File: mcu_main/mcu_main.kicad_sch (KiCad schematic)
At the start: 23 parts, among them SW1 SW_Push_Dual, SW2 SW_Push_Dual, U1 ESP32-S3-WROOM-1, U3 SGM2212-3.3, U5 SGM2212-2.8

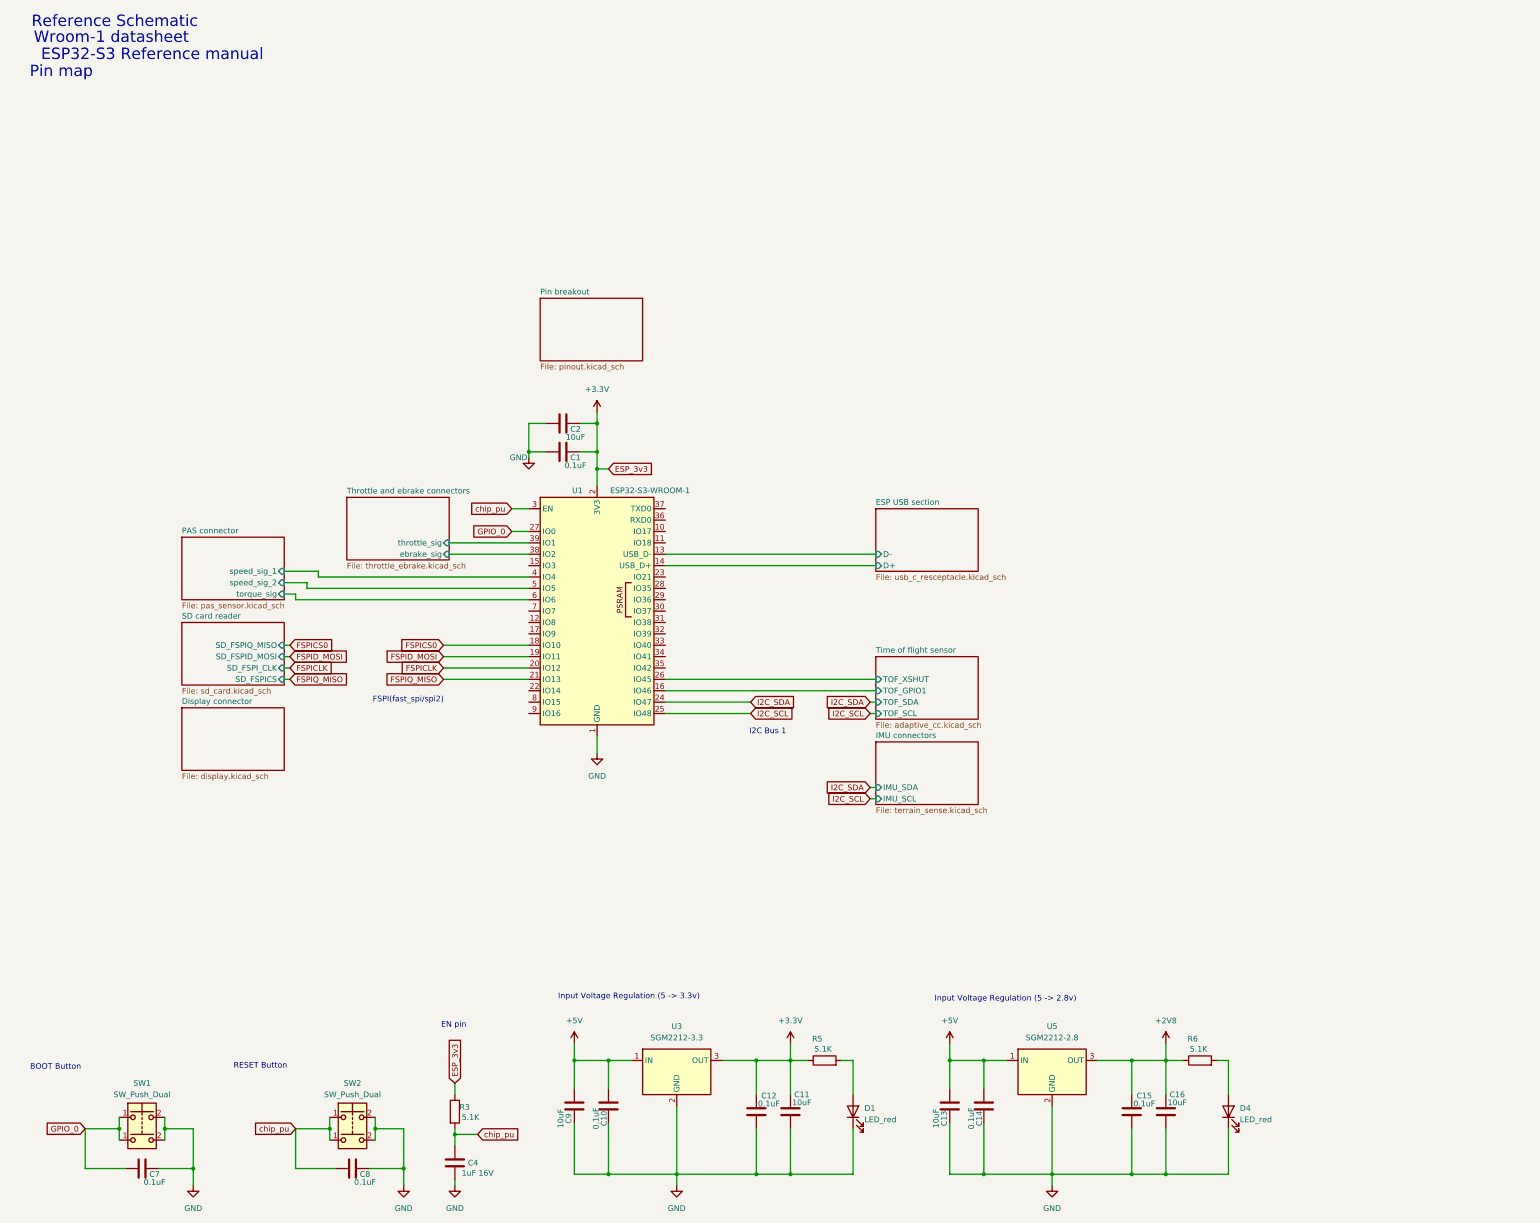
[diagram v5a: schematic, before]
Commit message: Added connections for the display SPI
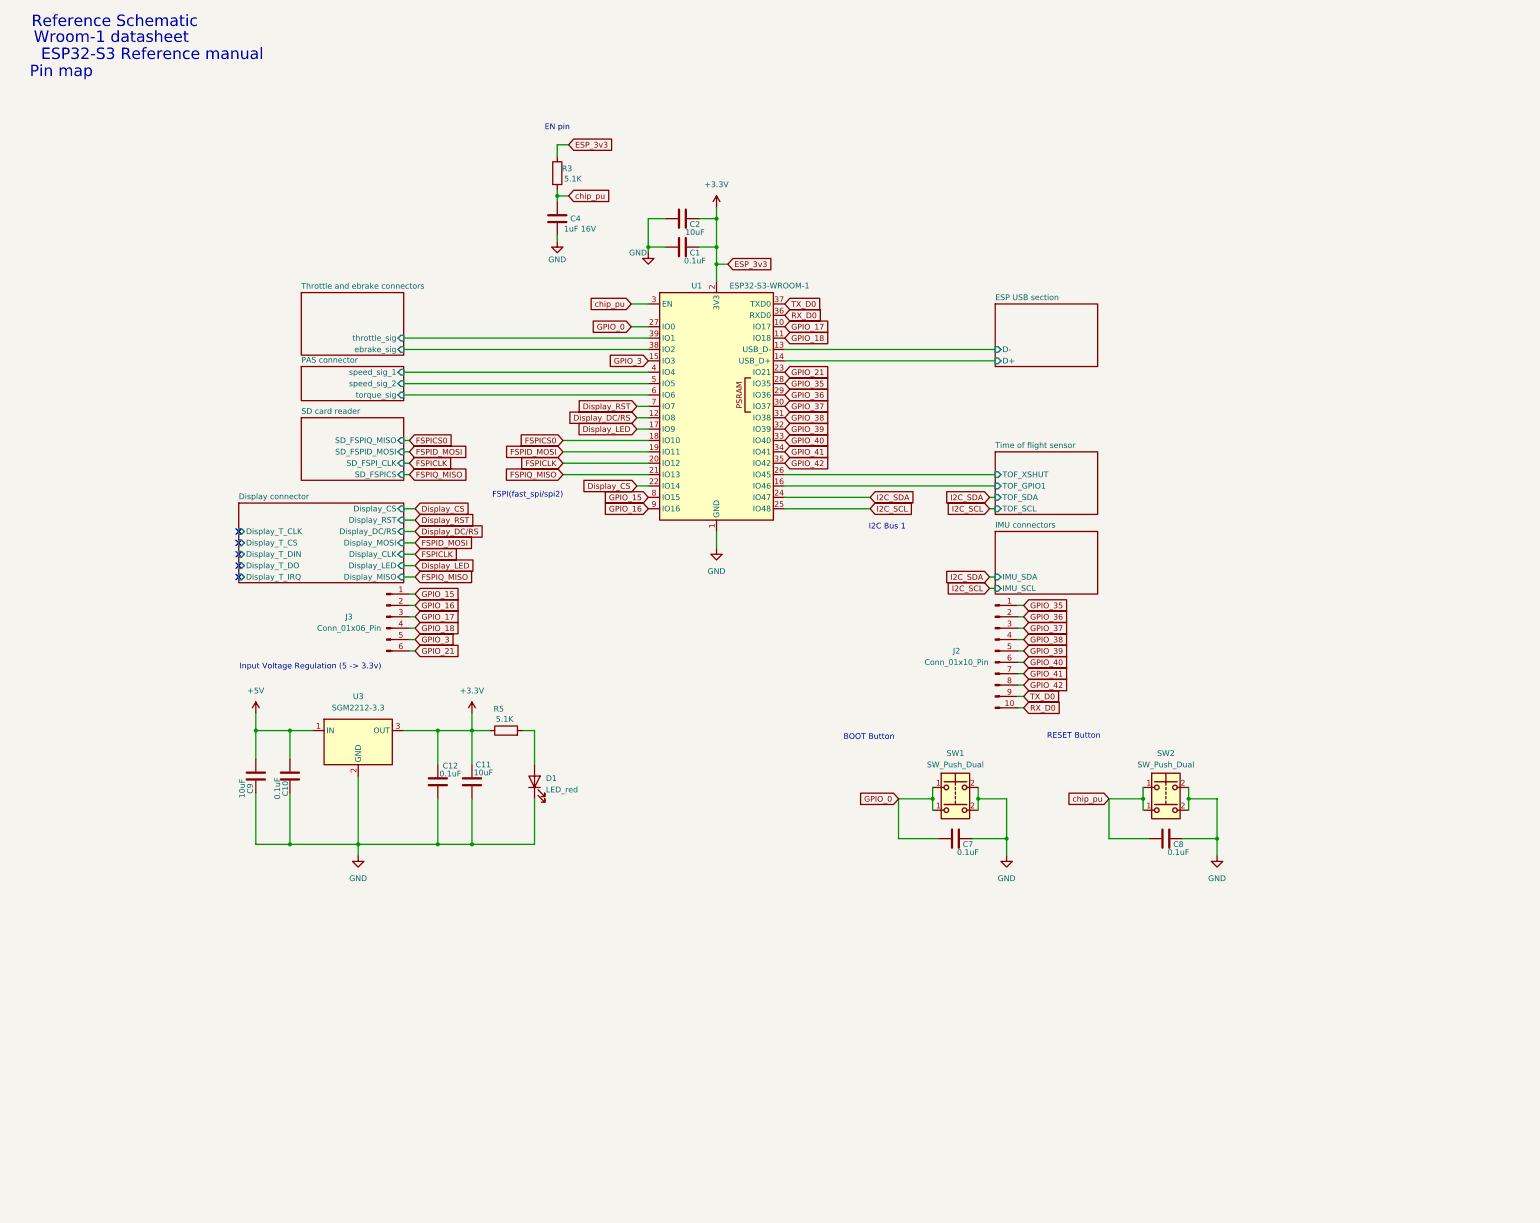
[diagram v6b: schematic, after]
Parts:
- removed C13, C16: 10uF, Capacitor_SMD:C_0603_1608Metric_Pad1.08x0.95mm_HandSolder, symbol Device:C
- removed C14, C15: 0.1uF, Capacitor_SMD:C_0603_1608Metric_Pad1.08x0.95mm_HandSolder, symbol Device:C
- removed D4: LED_red, LED_SMD:LED_0603_1608Metric_Pad1.05x0.95mm_HandSolder, symbol Device:LED
- removed R6: 5.1K, Resistor_SMD:R_0805_2012Metric_Pad1.20x1.40mm_HandSolder, symbol Device:R
- removed U5: SGM2212-2.8, Package_TO_SOT_SMD:SOT-223-3_TabPin2, symbol Regulator_Linear:LT1963AxST-1.5
- added J2: Conn_01x10_Pin, Connector_Molex:Molex_KK-254_AE-6410-10A_1x10_P2.54mm_Vertical, symbol Connector:Conn_01x10_Pin
- added J3: Conn_01x06_Pin, Connector_Molex:Molex_KK-254_AE-6410-06A_1x06_P2.54mm_Vertical, symbol Connector:Conn_01x06_Pin
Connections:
- net GPIO_17: now reaches U1.10 (IO17)
- net GPIO_17: now also J3.3 (Pin_3)
- net GPIO_18: now reaches U1.11 (IO18)
- net GPIO_18: now also J3.4 (Pin_4)
- net Display_DC/RS: now reaches U1.12 (IO8)
- net GPIO_3: now reaches U1.15 (IO3)
- net GPIO_3: now also J3.5 (Pin_5)
- net Display_LED: now reaches U1.17 (IO9)
- net Display_CS: now reaches U1.22 (IO14)
- net GPIO_21: now reaches U1.23 (IO21)
- net GPIO_21: now also J3.6 (Pin_6)
- net GPIO_35: now reaches U1.28 (IO35)
- net GPIO_35: now also J2.1 (Pin_1)
- net GPIO_36: now reaches U1.29 (IO36)
- net GPIO_36: now also J2.2 (Pin_2)
- net GPIO_37: now reaches U1.30 (IO37)
- net GPIO_37: now also J2.3 (Pin_3)
- net GPIO_38: now reaches U1.31 (IO38)
- net GPIO_38: now also J2.4 (Pin_4)
- net GPIO_39: now reaches U1.32 (IO39)
- net GPIO_39: now also J2.5 (Pin_5)
- net GPIO_40: now reaches U1.33 (IO40)
- net GPIO_40: now also J2.6 (Pin_6)
- net GPIO_41: now reaches U1.34 (IO41)
- net GPIO_41: now also J2.7 (Pin_7)
- net GPIO_42: now reaches U1.35 (IO42)
- net GPIO_42: now also J2.8 (Pin_8)
- net RX_D0: now reaches U1.36 (RXD0)
- net RX_D0: now also J2.10 (Pin_10)
- net TX_D0: now reaches U1.37 (TXD0)
- net TX_D0: now also J2.9 (Pin_9)
- net Display_RST: now reaches U1.7 (IO7)
- net GPIO_15: now reaches U1.8 (IO15)
- net GPIO_15: now also J3.1 (Pin_1)
- net GPIO_16: now reaches U1.9 (IO16)
- net GPIO_16: now also J3.2 (Pin_2)
- no-connect marks 0 -> 5
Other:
- removed sheet Pin breakout
- sheet Display connector ports: added Display_CLK, Display_CS, Display_DC/RS, Display_LED, Display_MISO, Display_MOSI, Display_RST, Display_T_CLK, Display_T_CS, Display_T_DIN, Display_T_DO, Display_T_IRQ; removed none
- note removed: "Input Voltage Regulation (5 -> 2.8v)"
- moved on the sheet: C1, C10, C11, C12, C2, C4, C7, C8, C9, D1, R3, R5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

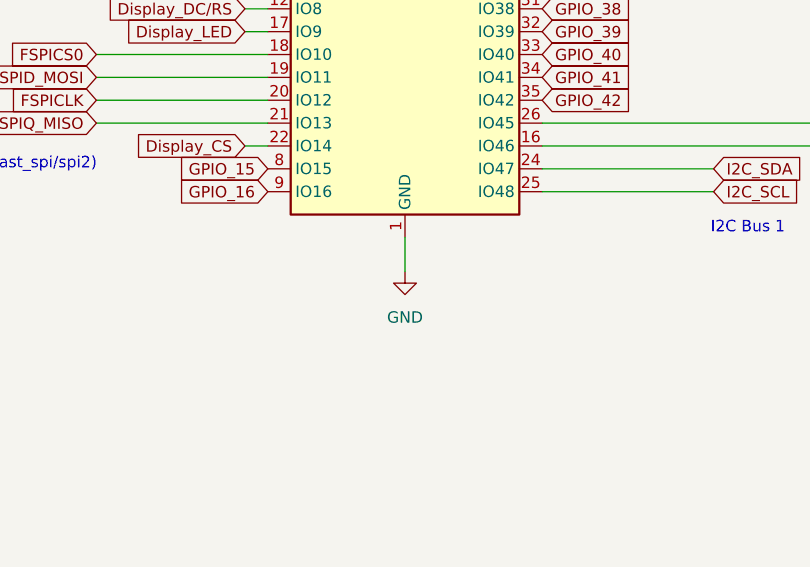
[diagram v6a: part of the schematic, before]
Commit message: ERC done and fixed
most of the stuff was fine, except needed to fix the power pins on the tvs diode symbol
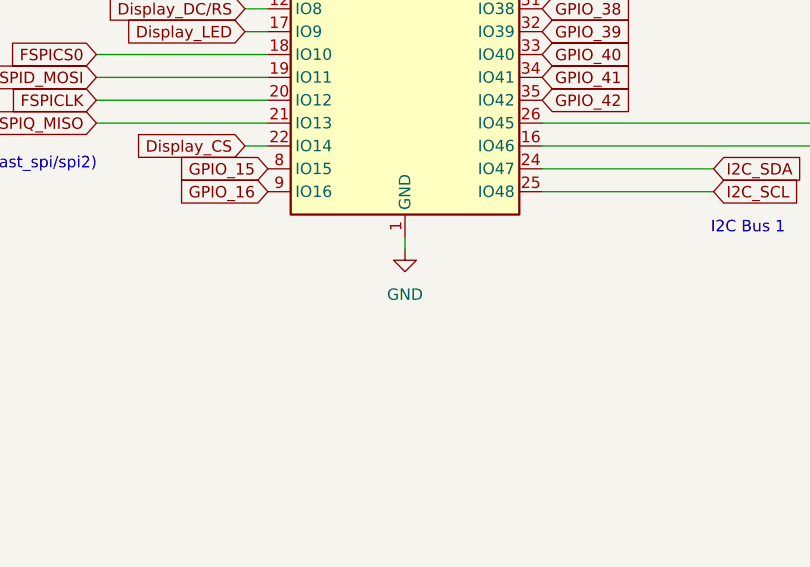
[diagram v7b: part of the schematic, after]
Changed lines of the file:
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@@
+	(wire
+		(pts
+			(xy 167.64 130.81) (xy 167.64 129.54)
+		)
+		(stroke
+			(width 0)
+			(type default)
+		)
+	)
 	(wire
 		(pts
@@
 	(wire
 		(pts
-			(xy 167.64 133.35) (xy 167.64 129.54)
-		)
-		(stroke
-			(width 0)
-			(type default)
-		)
-	)
-	(wire
-		(pts
 			(xy 97.79 124.46) (xy 100.33 124.46)
 		)
@@
 				(justify right)
 				(hide yes)
+			)
+		)
+	)
+	(rule_area
+		(polyline
+			(pts
+				(xy 134.6351 119.3433) (xy 118.1251 119.3433) (xy 118.1268 106.7591) (xy 134.6368 106.7591)
+			)
+			(stroke
+				(width 0)
+				(type dash)
+			)
+			(fill
+				(type none)
 			)
 		)
@@
 		(polyline
 			(pts
+				(xy 195.58 176.53) (xy 195.58 209.55) (xy 238.76 209.55) (xy 238.76 176.53)
+			)
+			(stroke
+				(width 0)
+				(type dash)
+			)
+			(fill
+				(type none)
+			)
+		)
+	)
+	(rule_area
+		(polyline
+			(pts
+				(xy 241.3 176.53) (xy 241.3 209.55) (xy 285.75 209.55) (xy 285.75 176.53)
+			)
+			(stroke
+				(width 0)
+				(type dash)
+			)
+			(fill
+				(type none)
+			)
+		)
+	)
+	(rule_area
+		(polyline
+			(pts
 				(xy 58.42 161.29) (xy 58.42 209.55) (xy 139.7 209.55) (xy 139.7 161.29)
 			)
@@
 			(pts
 				(xy 129.1488 40.6278) (xy 129.1489 71.1078) (xy 147.32 71.1199) (xy 147.3199 40.6399)
-			)
-			(stroke
-				(width 0)
-				(type dash)
-			)
-			(fill
-				(type none)
-			)
-		)
-	)
-	(rule_area
-		(polyline
-			(pts
-				(xy 241.3 176.53) (xy 241.3 209.55) (xy 285.75 209.55) (xy 285.75 176.53)
-			)
-			(stroke
-				(width 0)
-				(type dash)
-			)
-			(fill
-				(type none)
-			)
-		)
-	)
-	(rule_area
-		(polyline
-			(pts
-				(xy 134.6351 119.3433) (xy 118.1251 119.3433) (xy 118.1268 106.7591) (xy 134.6368 106.7591)
-			)
-			(stroke
-				(width 0)
-				(type dash)
-			)
-			(fill
-				(type none)
-			)
-		)
-	)
-	(rule_area
-		(polyline
-			(pts
-				(xy 195.58 176.53) (xy 195.58 209.55) (xy 238.76 209.55) (xy 238.76 176.53)
 			)
 			(stroke
@@
 	(symbol
 		(lib_id "power:GND")
-		(at 167.64 133.35 0)
+		(at 167.64 130.81 0)
 		(unit 1)
 		(exclude_from_sim no)
@@
 		(fields_autoplaced yes)
 		(property "Reference" "#PWR02"
-			(at 167.64 139.7 0)
+			(at 167.64 137.16 0)
 			(effects
 				(font
@@
 		)
 		(property "Value" "GND"
-			(at 167.64 138.43 0)
+			(at 167.64 135.89 0)
 			(effects
 				(font
@@
 		)
 		(property "Footprint" ""
-			(at 167.64 133.35 0)
+			(at 167.64 130.81 0)
 			(effects
 				(font
@@
 		)
 		(property "Datasheet" ""
-			(at 167.64 133.35 0)
+			(at 167.64 130.81 0)
 			(effects
 				(font
@@
 		)
 		(property "Description" "Power symbol creates a global label with name \"GND\" , ground"
-			(at 167.64 133.35 0)
-			(effects
-				(font
+			(at 167.64 130.81 0)
+			(effects
+				(font
